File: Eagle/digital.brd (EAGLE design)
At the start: 111.1 x 72.4 mm, 53 parts, among them IC1 MAX232, J1 USB+SHIELD

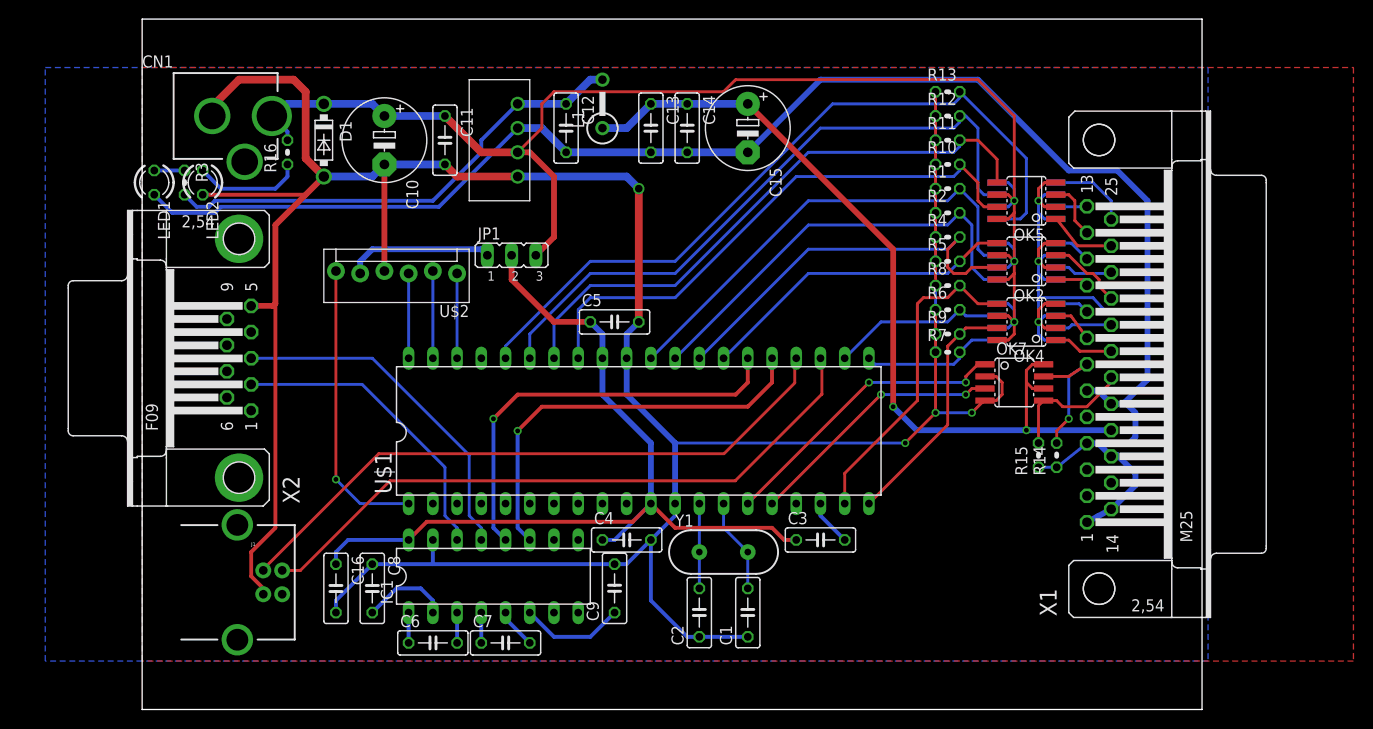
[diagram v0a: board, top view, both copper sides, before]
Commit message: Added ethernet module
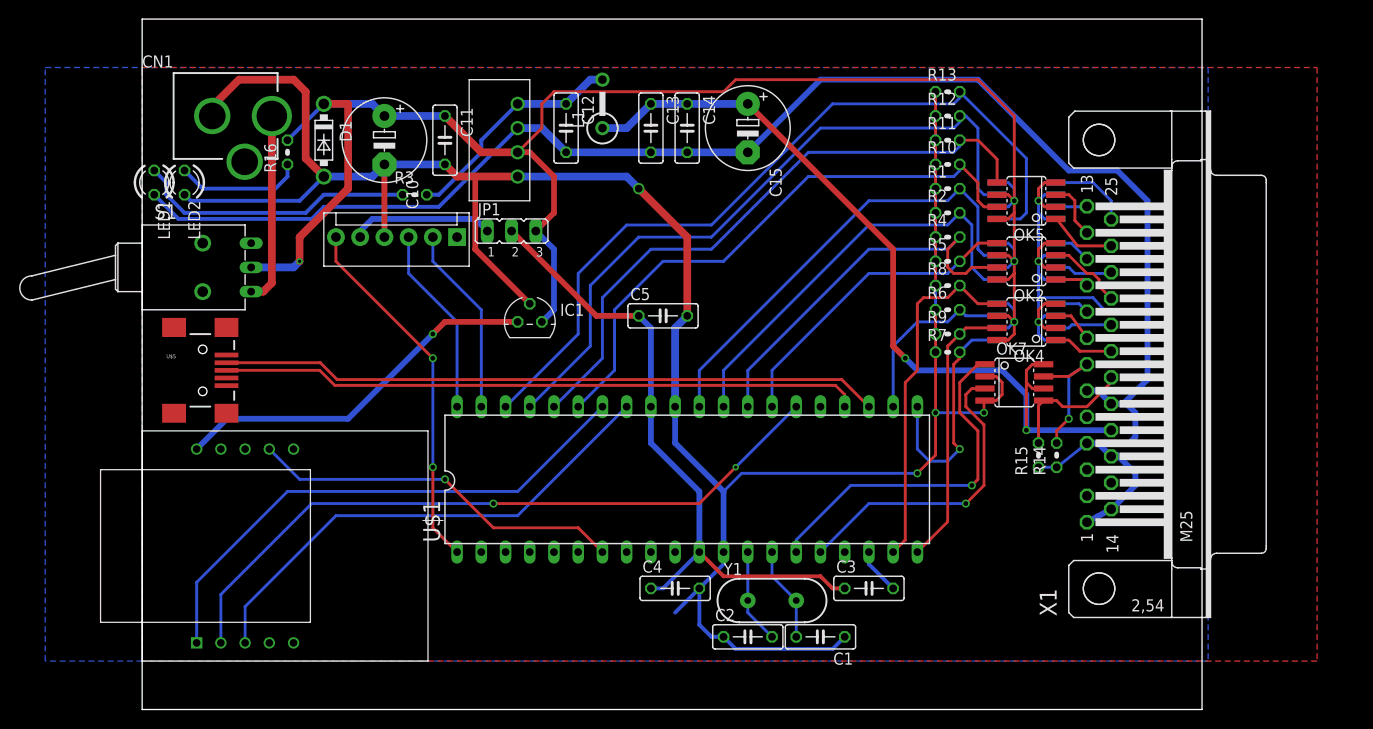
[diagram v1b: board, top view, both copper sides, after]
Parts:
- removed C16, C6, C7, C8, C9: 1uF, resistor:C050-025X075
- removed J1: USB+SHIELD, SparkFun-Connectors:USB-B-PTH
- removed X2: (no value), con-subd:F09HP
- added S1: (no value), switch:9070-1W
- added U$4: ENC28J60-H, modEEG:ENC28J60-H
- added U$5: USBSMD, SparkFun-Connectors:USB-MINIB
- IC1: value MAX232 -> L4931CZ33-AP; device maxim:DIL16 -> v-reg:TO92
- U$2: value PIC-ICSPPOLAR_LOCK -> PIC-ICSPPTH; device SparkFun-Connectors:MOLEX-1X6_LOCK -> SparkFun-Connectors:MOLEX-1X6
- moved IC1 26.9 mm to (40.6, 40.6)
- moved R3 24.2 mm to (28.6, 54.0), turned to 0 degrees
- moved C1 8.03 mm to (71.1, 7.62), turned to 180 degrees
- moved C4 7.18 mm to (55.9, 12.7)
- moved Y1 7.18 mm to (66.0, 11.4)
- moved C3 7.18 mm to (76.2, 12.7)
- moved U$1 7.18 mm to (57.1, 24.1)
- moved C2 5.68 mm to (63.5, 7.62), turned to 0 degrees
- moved C5 5.12 mm to (54.6, 41.3)
- moved U$2 3.81 mm to (33.0, 49.5)
- moved JP1 2.54 mm to (38.7, 50.2)
- moved LED2 1.90 mm to (4.45, 55.2)
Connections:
- removed net N$46: IC1.12, U$1.26
- removed net N$47: C8.2, IC1.2
- removed net N$48: C9.1, IC1.6
- removed net N$49: C6.2, IC1.3
- removed net N$50: C6.1, IC1.1
- removed net N$51: C7.1, IC1.4
- removed net N$52: C7.2, IC1.5
- removed net N$53: IC1.13, X2.3
- removed net N$54: IC1.14, X2.2
- new net N$3: U$1.26, U$4.P$2
- new net N$4: IC1.1, U$4.P$10
- new net N$42: U$1.34, U$4.P$1
- new net N$43: U$1.7, U$4.P$7
- net +5V/2: now also IC1.3, S1.2; no longer CN1.PWR
- net DGND: now also IC1.2, S1.3, S1.B, S1.B1, U$4.P$9; no longer C16.2, C8.1, C9.2, IC1.15, J1.GND, J1.S1, J1.S2, X2.5
- net N$33: now also U$1.35; no longer U$1.33
- net N$34: now also U$1.36; no longer U$1.34
- net N$35: now also U$1.37; no longer U$1.35
- net N$36: now also U$1.38; no longer U$1.36
- net N$44: now also CN1.PWR, S1.1; no longer IC1.11, U$1.25
- net N$45: no longer C16.1, IC1.16
- net N$6: now also U$1.33, U$4.P$3; no longer U$1.38, U$2.1
- net USB_N: now also U$5.D-; no longer J1.D-
- net USB_P: now also U$5.D+; no longer J1.D+
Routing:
- net N$3: track 0.00 -> 73.6 mm, vias 0 -> 2
- net DGND: track 300.3 -> 241.7 mm
- net N$42: track 0.00 -> 56.5 mm
- net N$46: track 44.0 -> 0.00 mm, vias 1 -> 0
- net N$6: track 8.89 -> 52.5 mm
- net N$43: track 0.00 -> 39.4 mm, vias 0 -> 1
- net N$4: track 0.00 -> 39.2 mm, vias 0 -> 1
- net N$53: track 36.5 -> 0.00 mm
- net N$54: track 32.1 -> 0.00 mm
- net +5V/2: track 156.0 -> 187.0 mm, vias 3 -> 4
- net N$26: track 50.6 -> 24.2 mm
- net N$45: track 94.2 -> 67.9 mm
- net N$28: track 3.18 -> 29.4 mm
- net N$44: track 43.3 -> 20.1 mm, vias 1 -> 0
- net N$8: track 8.89 -> 19.9 mm
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
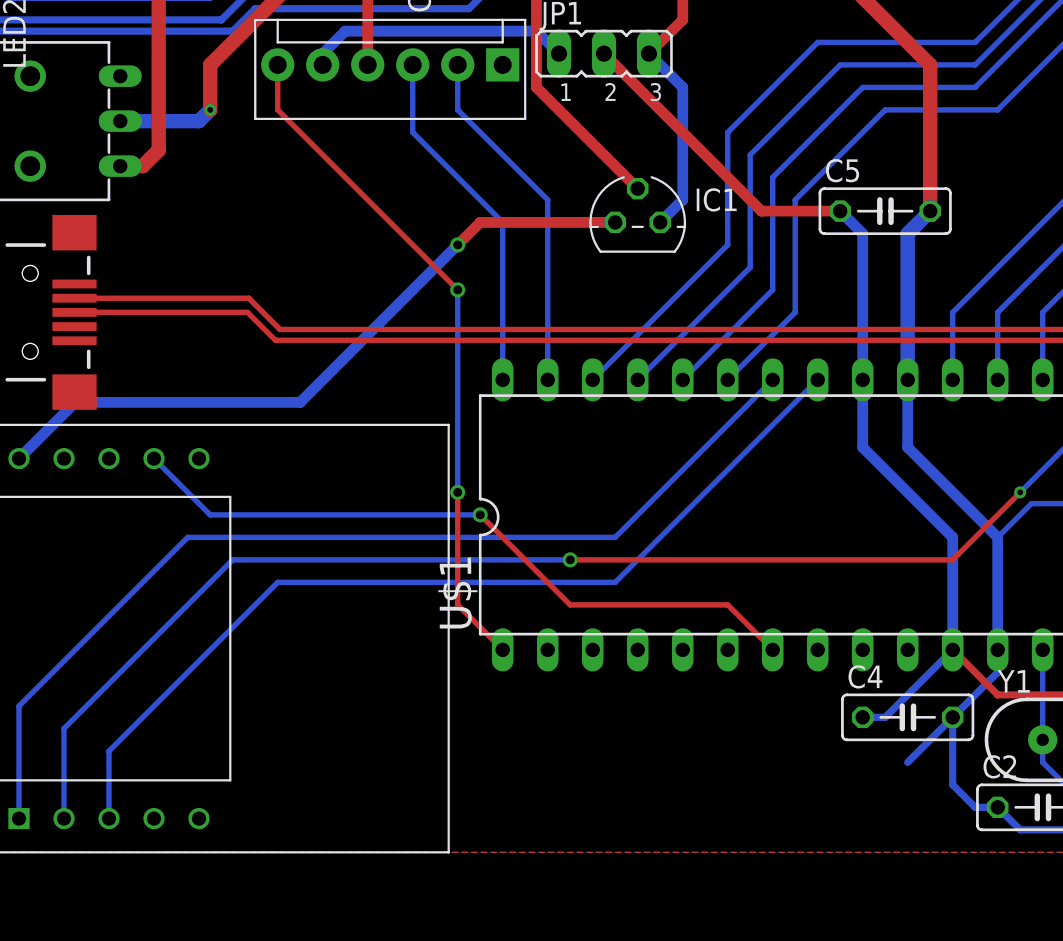
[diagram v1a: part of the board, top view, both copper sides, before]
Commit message: Added level shifting
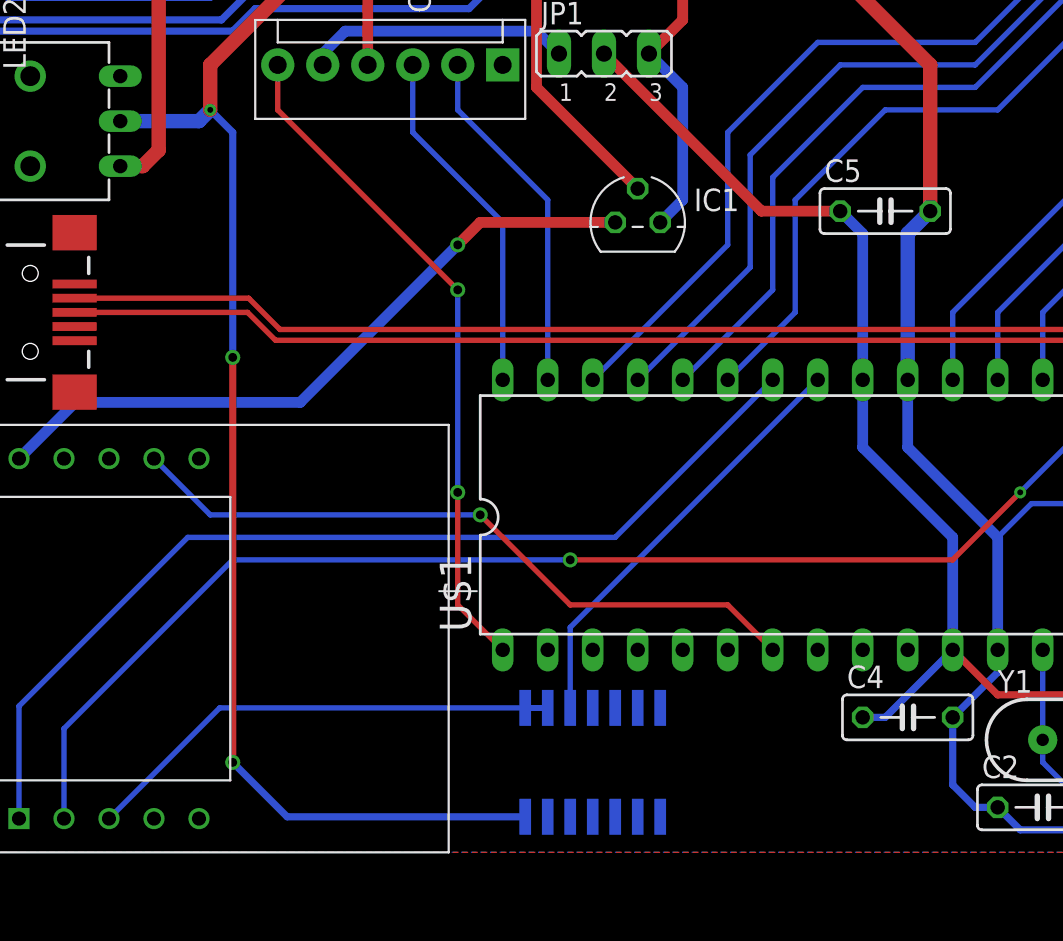
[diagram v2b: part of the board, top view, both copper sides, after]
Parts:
- added IC2: 74HCT08D, 74xx-eu:SO14
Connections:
- new net N$46: IC2.1, IC2.2, U$4.P$3
- net +5V/2: now also IC2.14
- net DGND: now also IC2.7
- net N$6: now also IC2.3; no longer U$4.P$3
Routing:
- net +5V/2: track 187.0 -> 242.2 mm, vias 4 -> 6
- net N$46: track 0.00 -> 28.6 mm
- net N$6: track 52.5 -> 24.3 mm
- net DGND: track 241.7 -> 238.1 mm
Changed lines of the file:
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@@
 </element>
 <element name="S1" library="switch" package="9070-1W" value="" x="6.35" y="46.355"/>
+<element name="IC2" library="74xx-eu" package="SO14" value="74HCT08D" x="38.1" y="10.16" rot="MR180"/>
 </elements>
 <signals>
@@
 <wire x1="17.145" y1="57.785" x2="19.05" y2="55.88" width="0.8128" layer="1"/>
 <wire x1="25.4" y1="49.53" x2="25.4" y2="57.15" width="0.6096" layer="1"/>
-<wire x1="55.88" y1="10.16" x2="58.42" y2="12.7" width="0.4064" layer="16"/>
 <wire x1="60.96" y1="7.62" x2="62.23" y2="6.35" width="0.4064" layer="16"/>
 <wire x1="62.23" y1="6.35" x2="72.39" y2="6.35" width="0.4064" layer="16"/>
@@
 <wire x1="5.08" y1="53.34" x2="16.51" y2="53.34" width="0.4064" layer="16"/>
 <wire x1="16.51" y1="53.34" x2="19.05" y2="55.88" width="0.4064" layer="16"/>
+<contactref element="IC2" pad="7"/>
 </signal>
 <signal name="N$26">
@@
 <wire x1="21.59" y1="63.5" x2="19.05" y2="63.5" width="0.8128" layer="1"/>
 <wire x1="15.24" y1="59.69" x2="19.05" y2="63.5" width="0.4064" layer="16"/>
+<contactref element="IC2" pad="14"/>
+<wire x1="34.29" y1="7.0866" x2="20.8534" y2="7.0866" width="0.4064" layer="16"/>
+<wire x1="20.8534" y1="7.0866" x2="17.78" y2="10.16" width="0.4064" layer="16"/>
+<via x="17.78" y="10.16" extent="1-16" drill="0.5"/>
+<wire x1="17.78" y1="10.16" x2="17.78" y2="33.02" width="0.4064" layer="1"/>
+<via x="17.78" y="33.02" extent="1-16" drill="0.5"/>
+<wire x1="17.78" y1="33.02" x2="17.78" y2="45.72" width="0.4064" layer="16"/>
+<wire x1="17.78" y1="45.72" x2="16.51" y2="46.99" width="0.4064" layer="16"/>
 </signal>
 <signal name="N$10">
@@
 <signal name="N$6">
 <contactref element="U$1" pad="33"/>
-<contactref element="U$4" pad="P$3"/>
-<wire x1="10.795" y1="6.985" x2="10.795" y2="10.795" width="0.3048" layer="16"/>
-<wire x1="10.795" y1="10.795" x2="20.32" y2="20.32" width="0.3048" layer="16"/>
-<wire x1="20.32" y1="20.32" x2="39.37" y2="20.32" width="0.3048" layer="16"/>
-<wire x1="39.37" y1="20.32" x2="50.8" y2="31.75" width="0.3048" layer="16"/>
+<contactref element="IC2" pad="3"/>
+<wire x1="50.8" y1="31.75" x2="36.83" y2="17.78" width="0.3048" layer="16"/>
+<wire x1="36.83" y1="17.78" x2="36.83" y2="13.2334" width="0.3048" layer="16"/>
 </signal>
 <signal name="N$42">
@@
 <wire x1="12.7" y1="43.815" x2="11.43" y2="43.815" width="0.8128" layer="1"/>
 </signal>
+<signal name="N$46">
+<contactref element="U$4" pad="P$3"/>
+<contactref element="IC2" pad="2"/>
+<contactref element="IC2" pad="1"/>
+<wire x1="34.29" y1="13.2334" x2="35.56" y2="13.2334" width="0.3048" layer="16"/>
+<wire x1="35.56" y1="13.2334" x2="17.0434" y2="13.2334" width="0.3048" layer="16"/>
+<wire x1="17.0434" y1="13.2334" x2="10.795" y2="6.985" width="0.3048" layer="16"/>
+</signal>
 </signals>

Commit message: Board updates
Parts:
- moved OK5 2.54 mm to (92.7, 50.8)
- moved OK6 2.54 mm to (92.7, 50.8)
- moved R7 2.54 mm to (84.5, 34.9)
- moved R8 2.54 mm to (84.5, 41.9)
- moved R14 2.54 mm to (95.9, 24.1)
- moved R15 2.54 mm to (94.0, 24.1)
- moved C1 2.54 mm to (71.1, 5.08)
- moved C2 2.54 mm to (63.5, 5.08)
- moved IC2 2.54 mm to (38.1, 7.62)
- moved U$4 2.54 mm to (0.00, 2.54)
- moved C10 2.54 mm to (25.4, 57.1)
- moved C11 2.54 mm to (31.8, 57.1)
- moved C12 2.54 mm to (44.5, 58.4)
- moved C13 2.54 mm to (53.3, 58.4)
- moved C14 2.54 mm to (57.1, 58.4)
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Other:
- board size 111.1 x 72.4 mm -> 111.1 x 67.3 mm

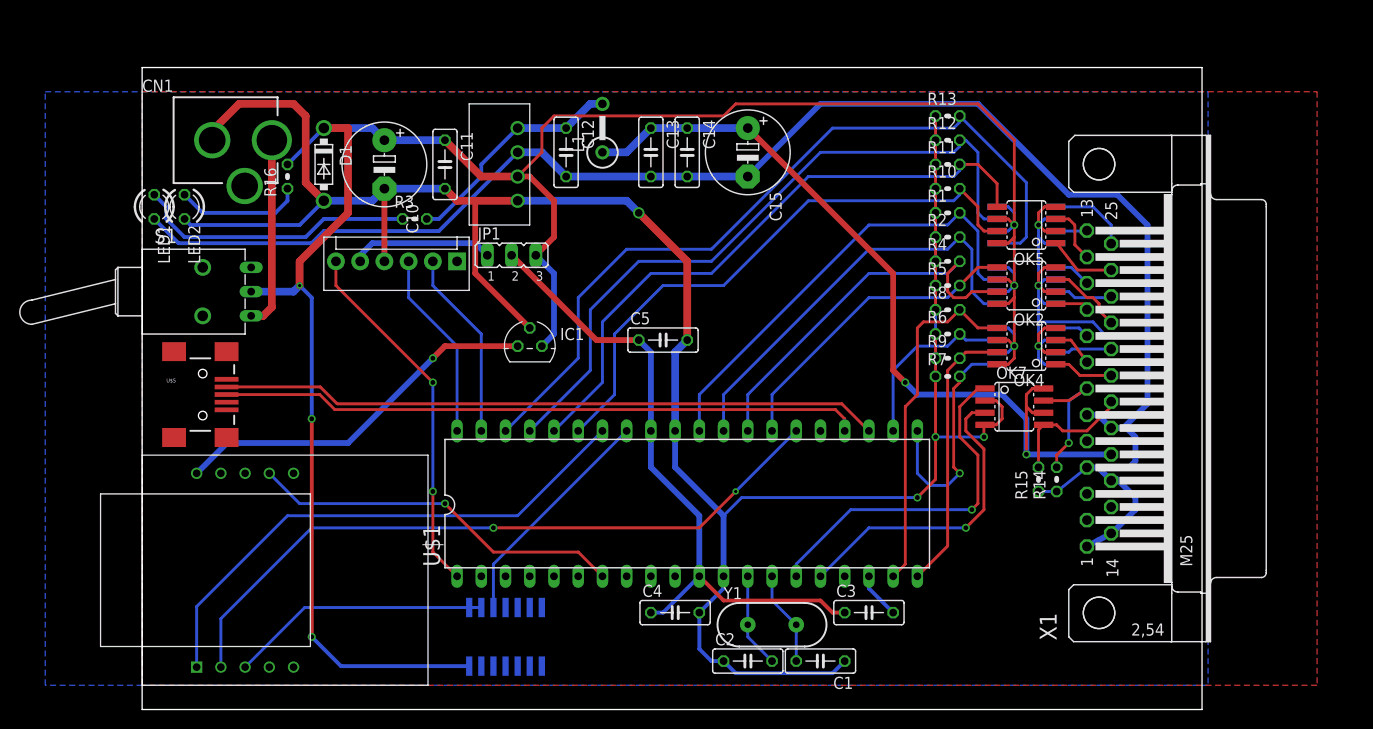
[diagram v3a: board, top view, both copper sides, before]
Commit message: Board shrink
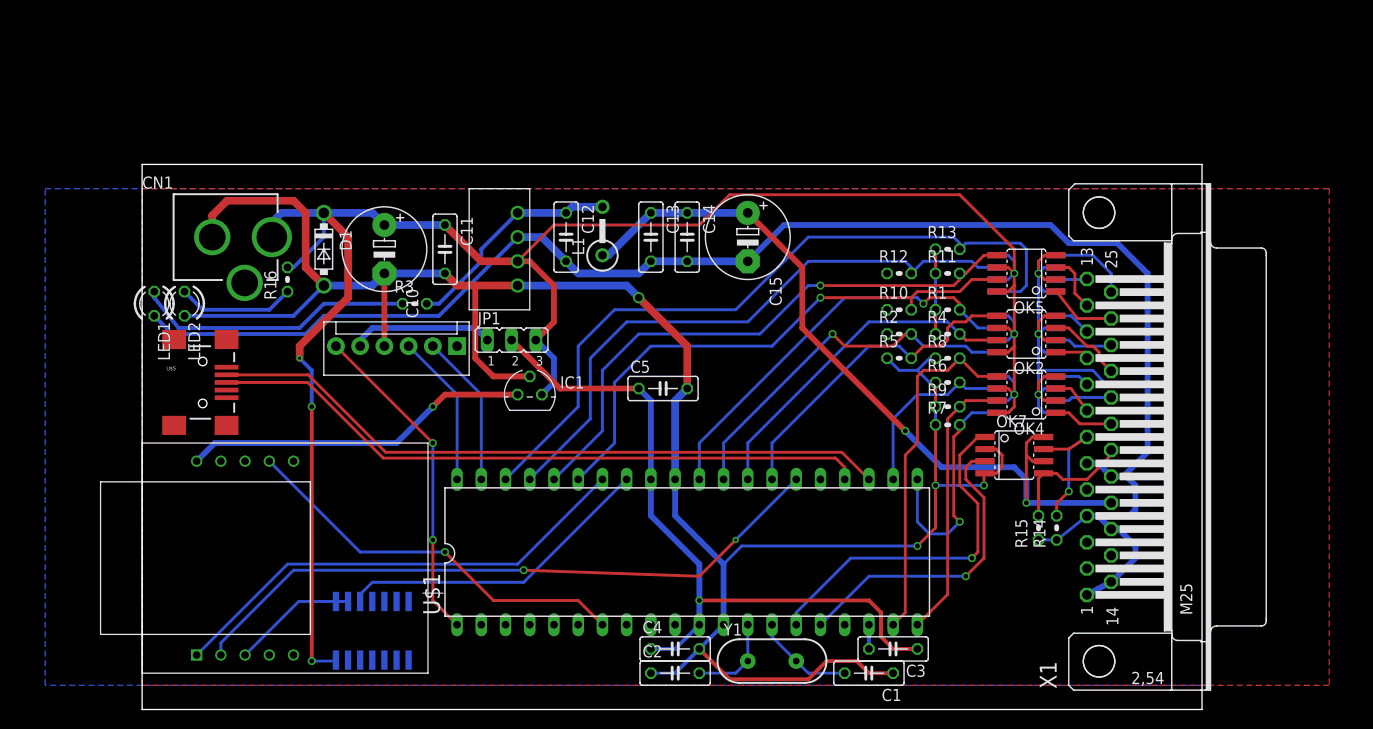
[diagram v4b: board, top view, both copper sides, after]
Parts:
- removed S1: (no value), switch:9070-1W
- moved R12 14.9 mm to (79.4, 45.7)
- moved IC2 14.0 mm to (24.1, 8.26)
- moved R13 14.0 mm to (84.5, 48.3)
- moved R10 13.7 mm to (79.4, 41.9)
- moved R11 11.4 mm to (84.5, 45.7)
- moved R2 11.4 mm to (79.4, 39.4)
- moved L1 10.8 mm to (48.3, 50.2)
- moved R16 10.8 mm to (15.2, 45.1)
- moved R1 10.2 mm to (84.5, 41.9)
- moved CN1 10.2 mm to (0.00, 49.5)
- moved LED1 10.2 mm to (1.27, 42.5)
- moved LED2 10.2 mm to (4.45, 42.5)
- moved R5 9.16 mm to (79.4, 36.8)
- moved C10 8.89 mm to (25.4, 48.3)
- moved C11 8.89 mm to (31.8, 48.3)
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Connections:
- removed net N$44: CN1.PWR, S1.1
- net +5V/2: now also CN1.PWR; no longer S1.2
- net DGND: no longer S1.3, S1.B, S1.B1
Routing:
- net +5V/2: track 242.2 -> 212.4 mm
- net N$44: track 20.1 -> 0.00 mm
- net N$46: track 28.6 -> 14.4 mm
- net N$6: track 24.3 -> 33.7 mm
- net N$35: track 72.9 -> 63.9 mm
- net N$45: track 67.9 -> 75.4 mm, vias 0 -> 1
- net N$36: track 84.3 -> 77.4 mm
- net N$42: track 56.5 -> 50.2 mm
- net N$24: track 44.8 -> 39.1 mm, vias 0 -> 1
- net N$25: track 41.2 -> 36.0 mm
- net N$34: track 65.4 -> 60.3 mm, vias 0 -> 1
- net N$15: track 48.4 -> 43.6 mm, vias 0 -> 1
- net N$3: track 73.6 -> 69.0 mm
- net DGND: track 238.1 -> 234.0 mm
- net N$33: track 61.5 -> 57.6 mm, vias 0 -> 1
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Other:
- board size 111.1 x 67.3 mm -> 111.1 x 57.1 mm
